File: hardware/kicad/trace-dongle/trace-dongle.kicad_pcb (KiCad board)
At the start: 2 copper layers, 55 x 25 mm, 31 parts, among them J1 OBD-II 5-pad fallback row (12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, J2 1x6 2.54mm UART header, SW1 BOOT tact, U1 ESP32-C3-MINI-1-N4, U2 TJA1051T/3, U3 TPS54202DDCR

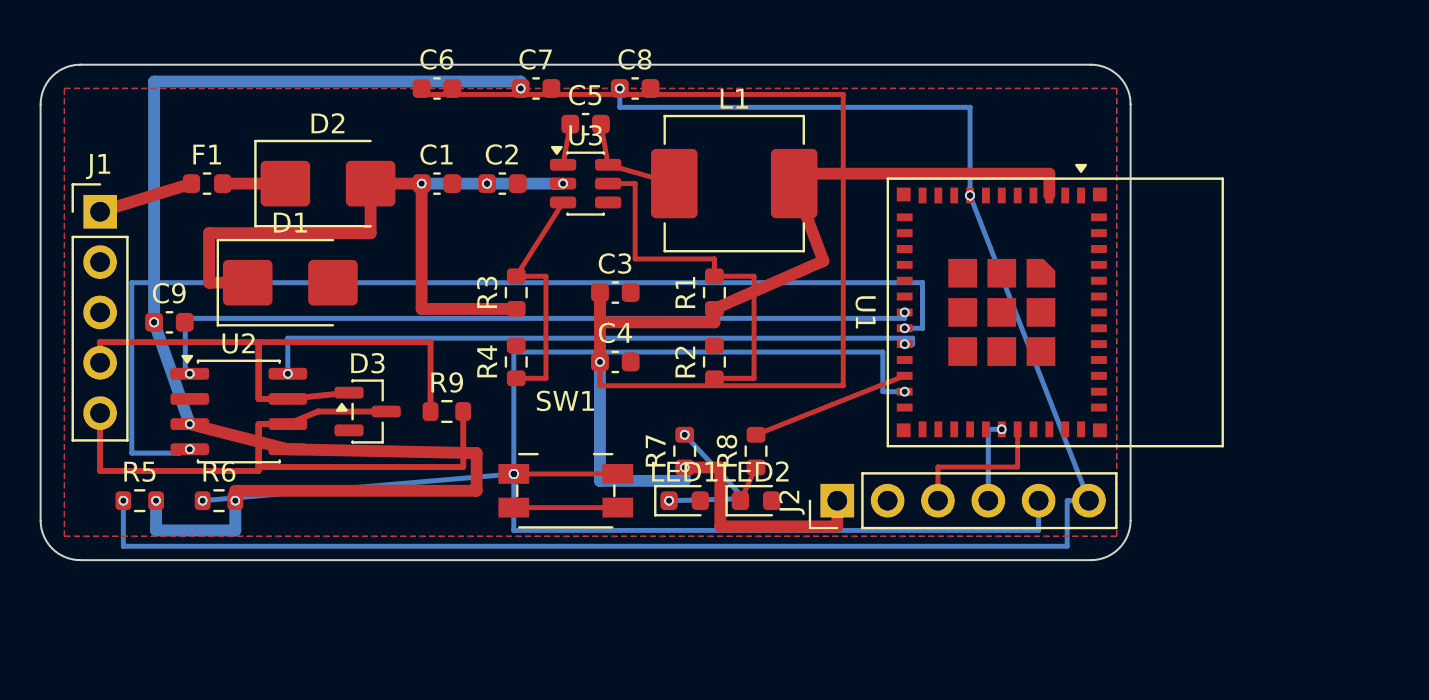
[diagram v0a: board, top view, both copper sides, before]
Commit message: P4c-hw HW2b: PCB wave 2 DONE — 62x30mm re-placement (root cause: wave-1 put U1-local parts across the board), corrected U3/D3 pin maps (4/6 and 3/3 wrong in wave 1 — LEAD binding maps), DRC 0 violations 0 unconnected exit 0 (LEAD re-verified), JLCPCB production set regenerated from clean board
Co-Authored-By: Claude Fable 5 <noreply@anthropic.com>
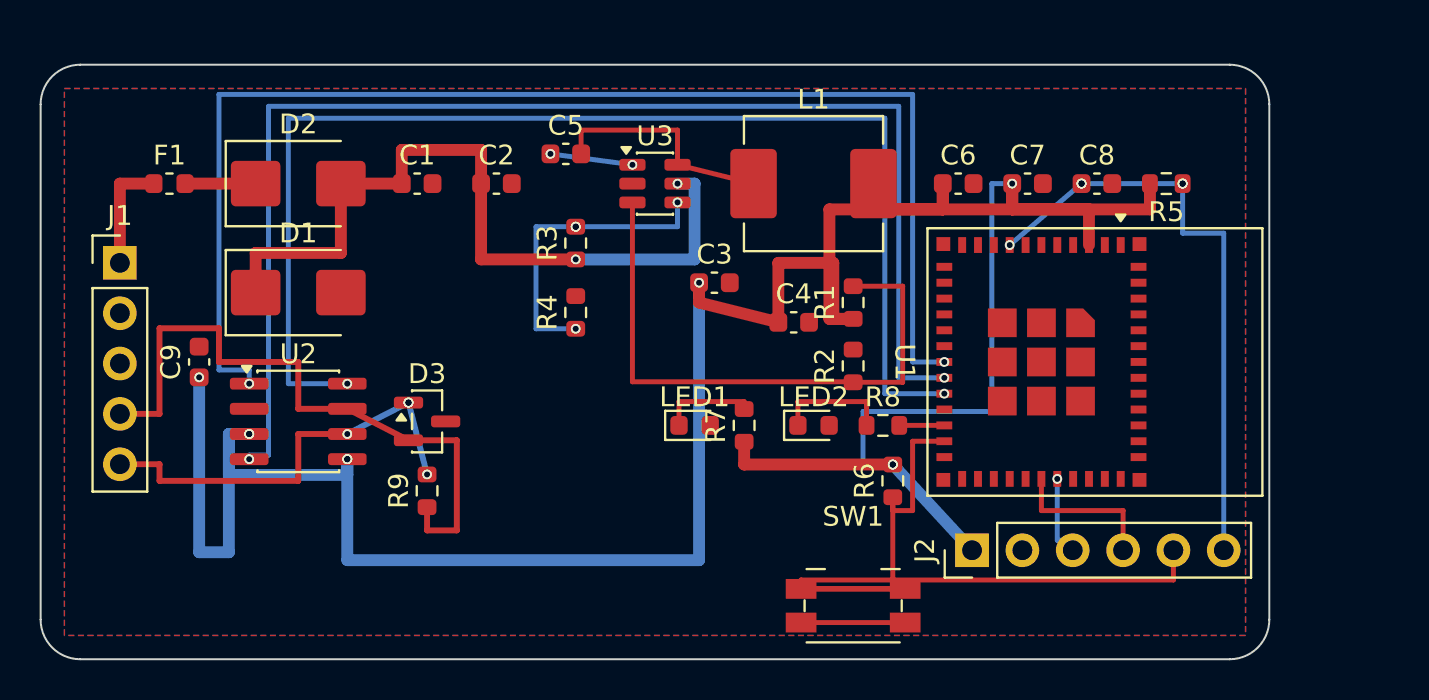
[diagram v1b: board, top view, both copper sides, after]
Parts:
- moved R5 54.2 mm to (56.8, 6.00), turned to 180 degrees
- moved R6 34.0 mm to (43.0, 21.0), turned to 90 degrees
- moved C6 26.7 mm to (46.3, 6.00)
- moved C7 25.3 mm to (49.8, 6.00)
- moved C8 23.8 mm to (53.3, 6.00)
- moved SW1 15.6 mm to (41.0, 27.3)
- moved C4 9.22 mm to (38.0, 13.0)
- moved J2 7.24 mm to (47.0, 24.5)
- moved R1 7.02 mm to (41.0, 12.0)
- moved R2 7.00 mm to (41.0, 15.2)
- moved R8 6.53 mm to (42.5, 18.2), turned to 0 degrees
- moved C3 5.02 mm to (34.0, 11.0)
- moved LED2 4.78 mm to (39.0, 18.2)
- moved R9 4.12 mm to (19.5, 21.5), turned to 90 degrees
- moved L1 4.00 mm to (39.0, 6.00)
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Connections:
- D3 pad 1: CANH -> CANL
- D3 pad 2: GND -> CANH
- D3 pad 3: CANL -> GND
- U3 pad 2: VIN_PROT -> GND
- U3 pad 3: EN_U3_NODE -> FB_NODE
- U3 pad 4: GND -> EN_U3_NODE
- U3 pad 5: FB_NODE -> VIN_PROT
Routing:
- net U1_EN: track 92.9 -> 30.4 mm
- net IO9_BOOT: track 79.7 -> 42.0 mm, vias 6 -> 0
- net CAN_S: track 34.0 -> 63.4 mm
- net CAN_TX: track 39.6 -> 66.2 mm
- net 3V3: track 181.4 -> 159.0 mm, vias 8 -> 10
- net CANL: track 36.6 -> 21.9 mm, vias 0 -> 4
- net CAN_RX: track 54.7 -> 66.6 mm
- net FB_NODE: track 19.2 -> 30.1 mm
- net SW_NODE: track 5.55 -> 11.8 mm
- net LED2_DRIVE: track 8.07 -> 2.27 mm
- net LED2_TOP: track 1.85 -> 5.86 mm
- net VIN_PROT: track 35.9 -> 39.6 mm, vias 4 -> 2
- net RXD0: track 4.28 -> 7.72 mm, vias 2 -> 0
- net LED1_TOP: track 8.19 -> 4.86 mm, vias 2 -> 0
- net TXD0: track 7.62 -> 4.38 mm, vias 0 -> 2
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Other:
- board size 55 x 25 mm -> 62 x 30 mm

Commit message: P4c-hw rev A3 remediation: all 12 items — verified TPS54202/TCAN330 pin maps (worker corrected LEAD's TCAN330 5/8 swap too), FB 22.1k, UVLO 133k (~7.8V), TCAN330DR 3.3V transceiver, D2/LED polarity, SMBJ18A pre-diode, LED2->IO7 + IO8 pullup, real 1210/0805 caps, 31/31 verified LCSC BOM (7 more fabricated ids caught), antenna keepout zone, spaced-hex + CAN response correlation in firmware; gates LEAD-verified: DRC 0/0, pio build 0, native 45/45 (board now 68x30)
Co-Authored-By: Claude Fable 5 <noreply@anthropic.com>
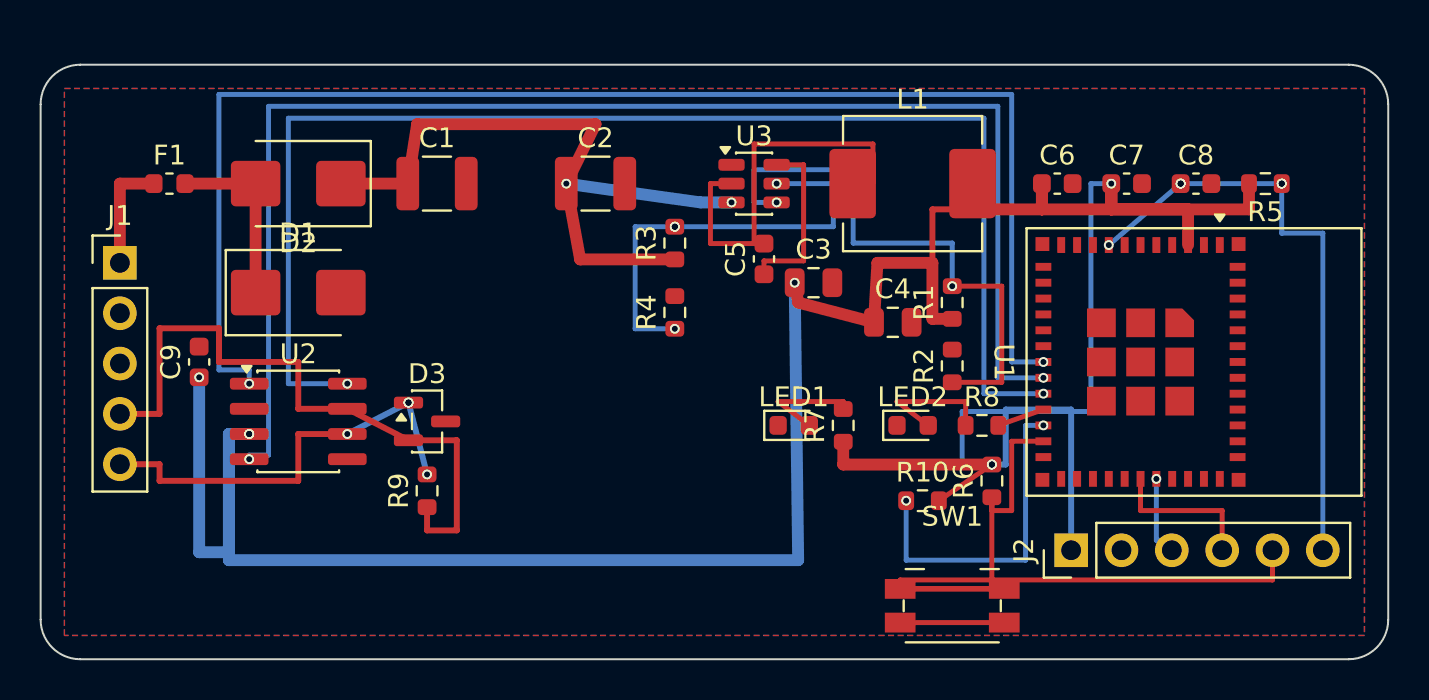
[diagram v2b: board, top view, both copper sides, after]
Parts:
- added R10: 10k (IO8 pullup, boot-mode high), R_0603_1608Metric, F.Cu at (44.5, 22.0)
- C1, C2: value 22uF/35V -> 10uF/50V X7R 1210; footprint C_0603_1608Metric -> C_1210_3225Metric
- C3, C4: value 22uF/10V -> 22uF/10V X7R 0805; footprint C_0603_1608Metric -> C_0805_2012Metric
- D1: value SMBJ24A -> SMBJ18A
- D2: value SS34 -> SS34B
- D3: value PESD2CAN -> PESD2CANFD24V-TR
- F1: value PTC 350mA -> PTC 350mA 16V
- J1: value OBD-II 5-pad fallback row (12V/GND/GND/CANH/CANL) -- C718401 pigtail fallback per DESIGN.md sec6 -> OBD-II 5-pad fallback row (12V/GND/GND/CANH/CANL) -- C2337 pigtail fallback, cut to 5 pins
- J2: value 1x6 2.54mm UART header -> 1x6 2.54mm UART header -- C2337, cut to 6 pins
- LED2: value amber (activity) -> amber/orange (activity)
- R2: value 13k (FB div lo) -> 22.1k (FB div lo)
- R3: value 100k (EN div hi) -> 133k (EN div hi)
- U2: value TJA1051T/3 -> TCAN330DR
- moved C5 11.3 mm to (36.5, 9.80), turned to 90 degrees
- moved C2 5.00 mm to (28.0, 6.00)
- moved C3 5.00 mm to (39.0, 11.0)
- moved C4 5.00 mm to (43.0, 13.0)
- moved C6 5.00 mm to (51.3, 6.00)
- moved C7 5.00 mm to (54.8, 6.00)
- moved C8 5.00 mm to (58.3, 6.00)
- moved J2 5.00 mm to (52.0, 24.5)
- moved L1 5.00 mm to (44.0, 6.00)
- moved LED1 5.00 mm to (38.0, 18.2)
- moved LED2 5.00 mm to (44.0, 18.2)
- moved R1 5.00 mm to (46.0, 12.0)
- moved R2 5.00 mm to (46.0, 15.2)
- moved R3 5.00 mm to (32.0, 9.00)
- moved R4 5.00 mm to (32.0, 12.5)
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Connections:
- D1 pad 1: VIN_PROT -> NET_FUSED
- D2 pad 1: NET_FUSED -> VIN_PROT
- D2 pad 2: VIN_PROT -> NET_FUSED
- LED1 pad 1: LED1_TOP -> GND
- LED1 pad 2: GND -> LED1_TOP
- LED2 pad 1: LED2_TOP -> GND
- LED2 pad 2: GND -> LED2_TOP
- U1 pad 21: (no net) -> LED2_DRIVE
- U1 pad 22: LED2_DRIVE -> IO8_PU
- U2 pad 5: 3V3 -> GND
- U3 pad 1: BST_NODE -> GND
- U3 pad 2: GND -> SW_NODE
- U3 pad 3: FB_NODE -> VIN_PROT
- U3 pad 4: EN_U3_NODE -> FB_NODE
- U3 pad 5: VIN_PROT -> EN_U3_NODE
- U3 pad 6: SW_NODE -> BST_NODE
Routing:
- net IO8_PU: track 0.00 -> 16.7 mm, vias 0 -> 2
- net 3V3: track 159.0 -> 173.0 mm, vias 10 -> 8
- net SW_NODE: track 11.8 -> 21.3 mm
- net EN_U3_NODE: track 15.5 -> 22.2 mm
- net NET_FUSED: track 3.56 -> 9.06 mm
- net CAN_S: track 63.4 -> 68.4 mm
- net CAN_RX: track 66.6 -> 71.6 mm
- net CAN_TX: track 66.2 -> 71.2 mm
- net BST_NODE: track 4.17 -> 8.89 mm, vias 2 -> 0
- net VIN_PROT: track 39.6 -> 35.8 mm
- net FB_NODE: track 30.1 -> 28.5 mm, vias 0 -> 2
- net LED2_TOP: track 5.86 -> 6.64 mm
- net LED1_TOP: track 4.86 -> 5.64 mm
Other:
- board size 62 x 30 mm -> 68 x 30 mm

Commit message: P4c-hw rev A4: final 7 fixes — F1 24V PTC (C910821), SW1 footprint aligned (EVQPUL_EVQPUC), enclosure 68mm re-render, full-antenna keepout + reroute, J1/J2 hand-solder (out of CPL, real Samtec parts), C2 adjacent to U3 VIN, UVLO 274k/44.2k (8.52/7.95V, hyst 0.57V) — DRC 0/0, BOM 31/31, all sources cited (Sonnet, LEAD gates green)
Co-Authored-By: Claude Fable 5 <noreply@anthropic.com>
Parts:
- F1: value PTC 350mA 16V -> PTC 350mA 24V; footprint Fuse_0603_1608Metric -> Fuse_0805_2012Metric
- J1: value OBD-II 5-pad fallback row (12V/GND/GND/CANH/CANL) -- C2337 pigtail fallback, cut to 5 pins -> OBD-II 5-pad fallback row (12V/GND/GND/CANH/CANL) -- hand-solder, TSW-105-07-T-S 1x5 header
- J2: value 1x6 2.54mm UART header -- C2337, cut to 6 pins -> 1x6 2.54mm UART header -- hand-solder, HTSW-106-07-T-S 1x6 header
- R3: value 133k (EN div hi) -> 274k (EN div hi)
- R4: value 24k (EN div lo) -> 44.2k (EN div lo)
- SW1: footprint Panasonic_EVQPUJ_EVQPUA -> Panasonic_EVQPUL_EVQPUC
- moved C2 4.51 mm to (31.8, 8.43), turned to -90 degrees
- moved R3 4.00 mm to (28.0, 9.00)
- moved R4 4.00 mm to (28.0, 12.5)
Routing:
- net U1_EN: track 30.4 -> 37.7 mm
- net EN_U3_NODE: track 22.2 -> 25.2 mm, vias 4 -> 2
- net VIN_PROT: track 35.8 -> 32.9 mm
- net IO9_BOOT: track 42.0 -> 43.2 mm

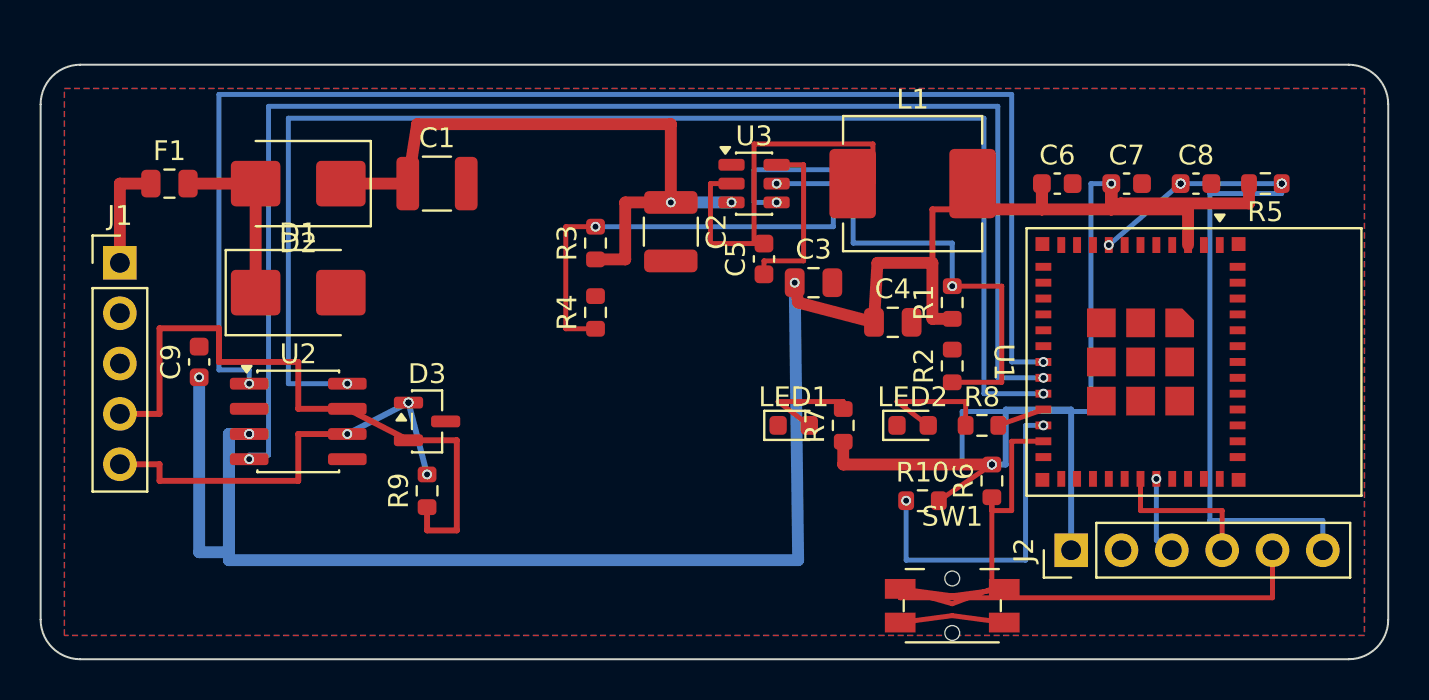
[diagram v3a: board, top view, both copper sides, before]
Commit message: P4c-hw: zero-warnings pass — via dedupe + THT-pad-coincident via removal (8 removed, holes_co_located x11 gone), 8 silkscreen refs repositioned; full-severity DRC: 0 violations 0 unconnected exit 0 (LEAD re-verified); production regenerated; kicad .history gitignored
Co-Authored-By: Claude Fable 5 <noreply@anthropic.com>
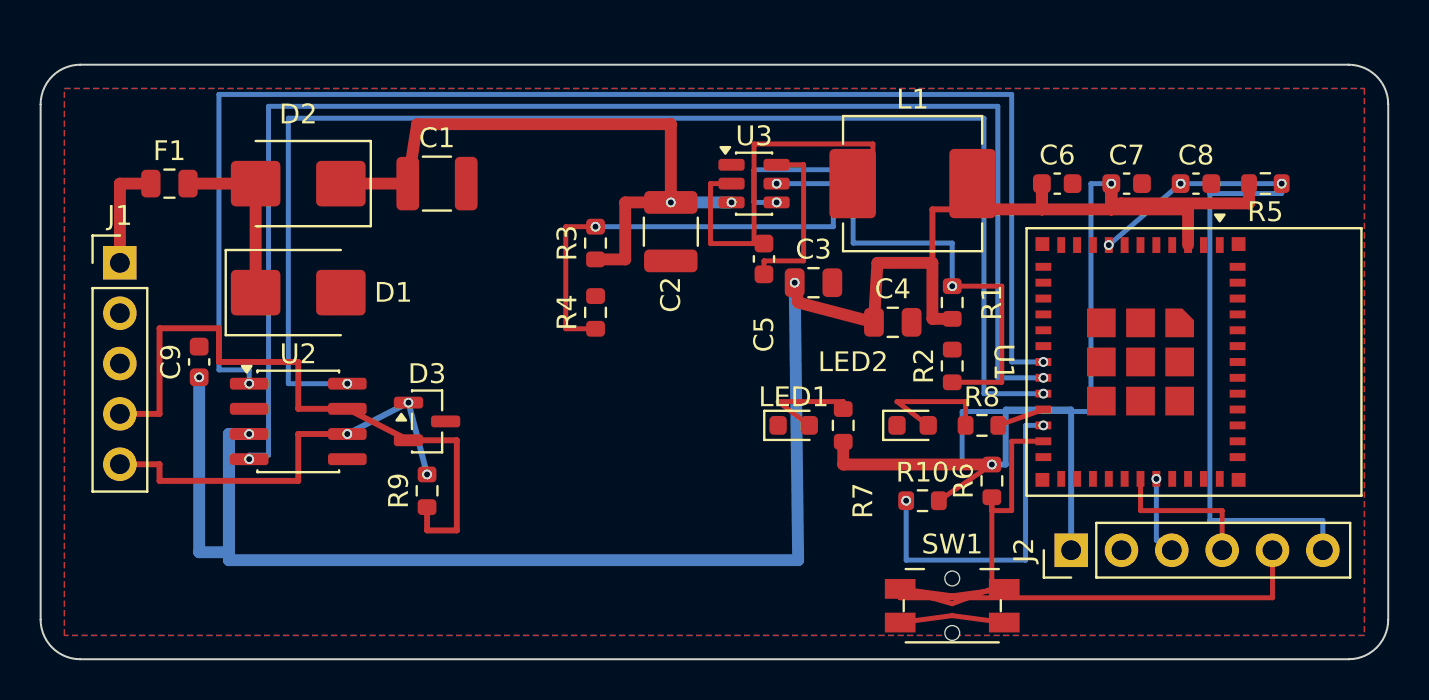
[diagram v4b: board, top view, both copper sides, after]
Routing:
- net 3V3: vias 8 -> 5
- net U1_EN: vias 6 -> 3
- net TXD0: vias 2 -> 1
- net CANL: vias 4 -> 3
